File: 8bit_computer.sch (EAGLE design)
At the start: 8 parts

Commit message: Added main clock initial description
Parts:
- R2: value (none) -> 1M
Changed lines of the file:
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@@
 <part name="C1" library="resistor" library_urn="urn:adsk.eagle:library:348" deviceset="C-EU" device="025-050X050" package3d_urn="urn:adsk.eagle:package:26152/1" value="100nF"/>
 <part name="C2" library="rcl" library_urn="urn:adsk.eagle:library:334" deviceset="CPOL-EU" device="E2-5" package3d_urn="urn:adsk.eagle:package:23346/2" value="1uF"/>
-<part name="R2" library="pot" library_urn="urn:adsk.eagle:library:331" deviceset="3RP/1610N" device="" package3d_urn="urn:adsk.eagle:package:22726/1"/>
+<part name="R2" library="pot" library_urn="urn:adsk.eagle:library:331" deviceset="3RP/1610N" device="" package3d_urn="urn:adsk.eagle:package:22726/1" value="1M"/>
 <part name="R3" library="resistor" library_urn="urn:adsk.eagle:library:348" deviceset="R-EU_" device="0204/5" package3d_urn="urn:adsk.eagle:package:25955/1" value="1k"/>
 <part name="LED1" library="eagle-ltspice" library_urn="urn:adsk.eagle:library:217" deviceset="LED_E" device="LD260" package3d_urn="urn:adsk.eagle:package:13313/1"/>
@@
 <instance part="R2" gate="G$1" x="-152.4" y="215.9" smashed="yes" rot="R270">
 <attribute name="NAME" x="-156.21" y="219.329" size="1.778" layer="95"/>
-<attribute name="VALUE" x="-156.21" y="219.71" size="1.778" layer="96"/>
+<attribute name="VALUE" x="-151.13" y="219.456" size="1.778" layer="96"/>
 </instance>
 <instance part="R3" gate="G$1" x="-139.7" y="215.9" smashed="yes" rot="R180">

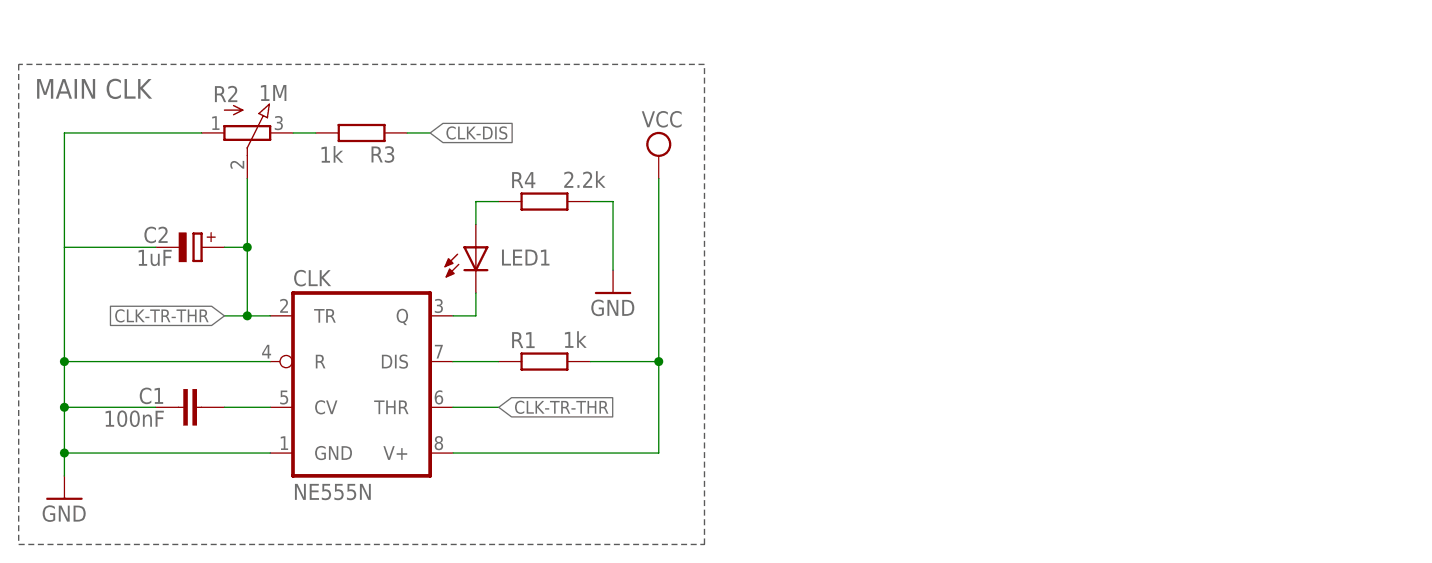
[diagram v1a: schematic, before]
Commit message: Stepping mode description
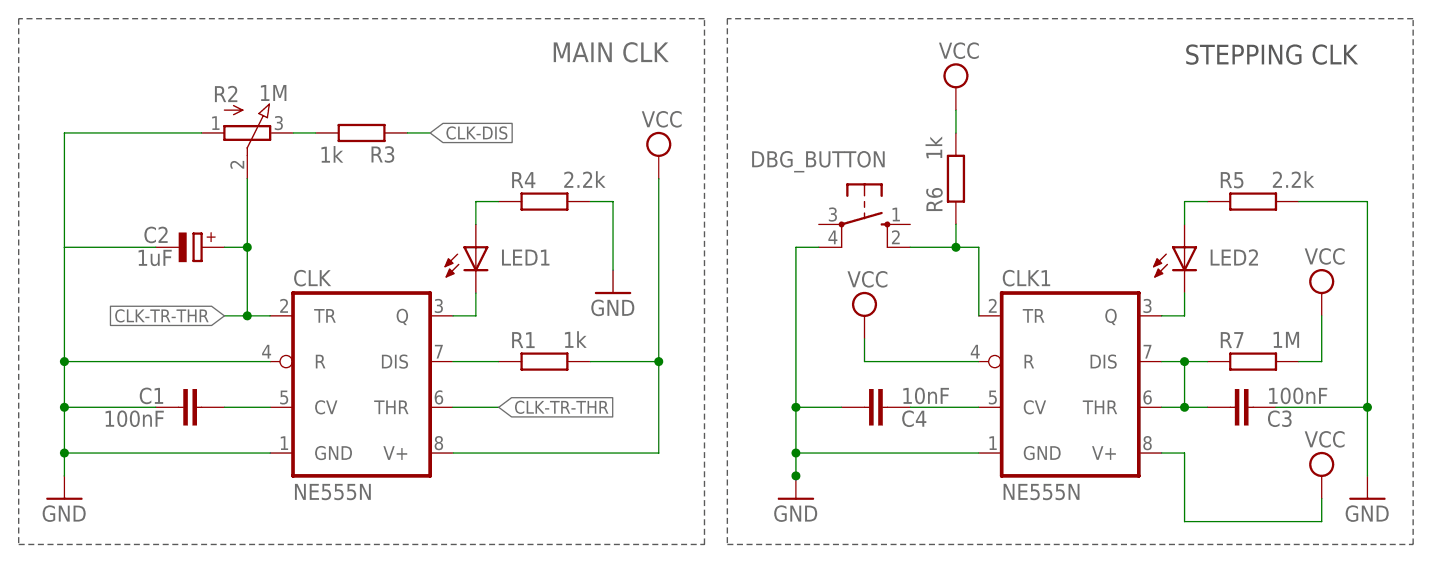
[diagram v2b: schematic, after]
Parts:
- added C3: 100nF, resistor:C-EU025-050X050
- added C4: 10nF, resistor:C-EU025-050X050
- added CLK1: NE555N, linear:NE555N
- added DBG_BUTTON: (no value), switch-omron:10-XX
- added LED2: (no value), eagle-ltspice:LED_ELD260
- added R5: 2.2k, resistor:R-EU_0204/5
- added R6: 1k, resistor:R-EU_0204/5
- added R7: 1M, resistor:R-EU_0204/5
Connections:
- new net N$1: CLK1.Q, LED2.C
- new net N$3: LED2.A, R5.1
- new net N$5: CLK1.TR, DBG_BUTTON.S1, R6.1
- new net N$6: C3.2, CLK1.DIS, CLK1.THR, R7.1
- new net N$7: C4.1, CLK1.CV
- net GND: now also C3.1, C4.2, CLK1.GND, DBG_BUTTON.P1, R5.2
- net VCC: now also CLK1.R, CLK1.V+, R6.2, R7.2
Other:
- note added: "STEPPING CLK"
